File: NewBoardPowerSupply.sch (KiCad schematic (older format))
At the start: 12 parts, among them IC1 ADM7172ACPZ-4.2-R7

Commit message: getting libraries to work
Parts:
- IC1: symbol ADM7172ACPZ-4.2-R7:ADM7172ACPZ-4.2-R7 -> laser-rescue:ADM7172ACPZ-4.2-R7-ADM7172ACPZ-4.2-R7
- IC?: symbol ADM7154ARDZ-3.3-R7:ADM7154ARDZ-3.3-R7 -> laser-rescue:ADM7154ARDZ-3.3-R7-ADM7154ARDZ-3.3-R7
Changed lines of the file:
@@
 $EndDescr
 $Comp
-L ADM7172ACPZ-4.2-R7:ADM7172ACPZ-4.2-R7 IC1
+L laser-rescue:ADM7172ACPZ-4.2-R7-ADM7172ACPZ-4.2-R7 IC1
 U 1 1 60C1104B
 P 4700 4750
@@
 $EndComp
 $Comp
-L ADM7154ARDZ-3.3-R7:ADM7154ARDZ-3.3-R7 IC?
+L laser-rescue:ADM7154ARDZ-3.3-R7-ADM7154ARDZ-3.3-R7 IC?
 U 1 1 60C11888
 P 8750 4750

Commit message: delete random cashe
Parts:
- IC1: symbol laser-rescue:ADM7172ACPZ-4.2-R7-ADM7172ACPZ-4.2-R7 -> ADM7172ACPZ-4.2-R7:ADM7172ACPZ-4.2-R7
- IC?: symbol laser-rescue:ADM7154ARDZ-3.3-R7-ADM7154ARDZ-3.3-R7 -> ADM7154ARDZ-3.3-R7:ADM7154ARDZ-3.3-R7
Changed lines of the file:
@@
 $EndDescr
 $Comp
-L laser-rescue:ADM7172ACPZ-4.2-R7-ADM7172ACPZ-4.2-R7 IC1
+L ADM7172ACPZ-4.2-R7:ADM7172ACPZ-4.2-R7 IC1
 U 1 1 60C1104B
 P 4700 4750
@@
 $EndComp
 $Comp
-L laser-rescue:ADM7154ARDZ-3.3-R7-ADM7154ARDZ-3.3-R7 IC?
+L ADM7154ARDZ-3.3-R7:ADM7154ARDZ-3.3-R7 IC?
 U 1 1 60C11888
 P 8750 4750
@@
 $EndComp
 $Comp
-L _NONAME_ #PWR?
-U 1 1 60C1B1D0
-P 8750 5050
-F 0 "#PWR?" H 8750 4800 50  0001 C CNN
-F 1 "GND" H 8755 4877 50  0000 C CNN
-F 2 "" H 8750 5050 50  0001 C CNN
-F 3 "" H 8750 5050 50  0001 C CNN
-	1    8750 5050
-	1    0    0    -1
-$EndComp
-$Comp
 L Device:C C?
 U 1 1 60C28A84
@@
 Wire Wire Line
 	8400 3900 3000 3900
-Wire Wire Line
-	3000 3900 3000 4850
 Connection ~ 8400 3900
-Connection ~ 3000 4850
 Wire Wire Line
 	9000 3900 10000 3900
 Connection ~ 9000 3900
+Connection ~ 3000 4850
+Wire Wire Line
+	3000 3900 3000 4850
+$Comp
+L power:GND #PWR?
+U 1 1 60C19547
+P 8750 5050
+F 0 "#PWR?" H 8750 4800 50  0001 C CNN
+F 1 "GND" H 8755 4877 50  0000 C CNN
+F 2 "" H 8750 5050 50  0001 C CNN
+F 3 "" H 8750 5050 50  0001 C CNN
+	1    8750 5050
+	1    0    0    -1
+$EndComp
 $EndSCHEMATC

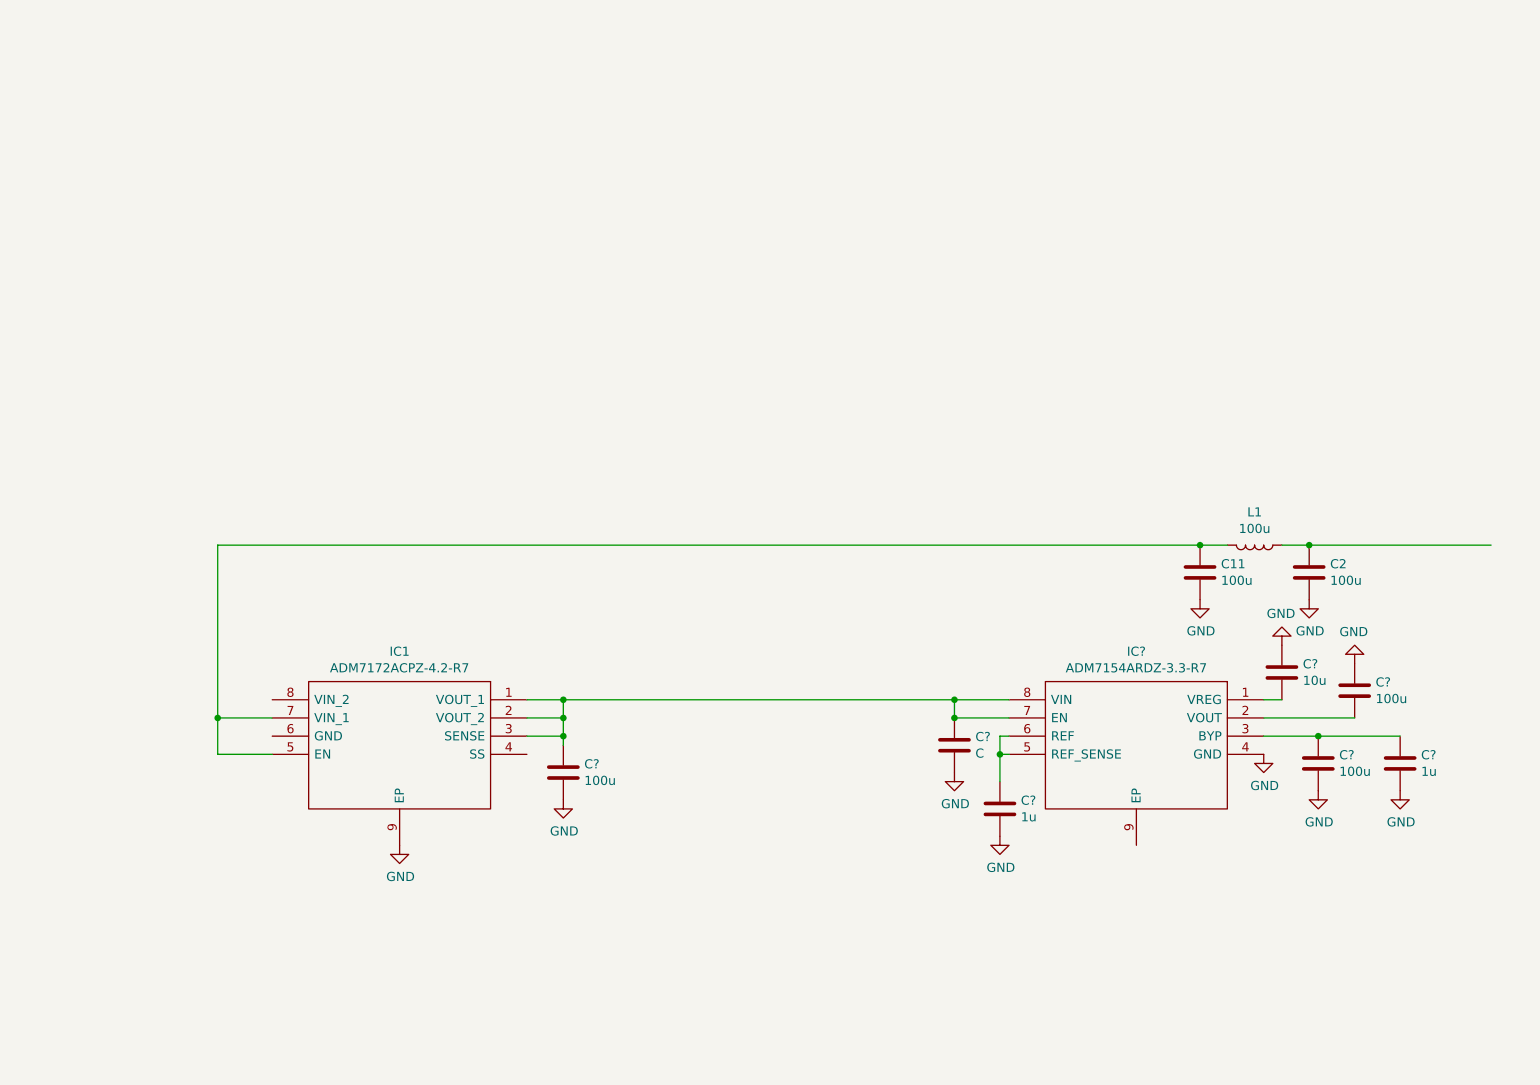
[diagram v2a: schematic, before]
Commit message: add LT1716
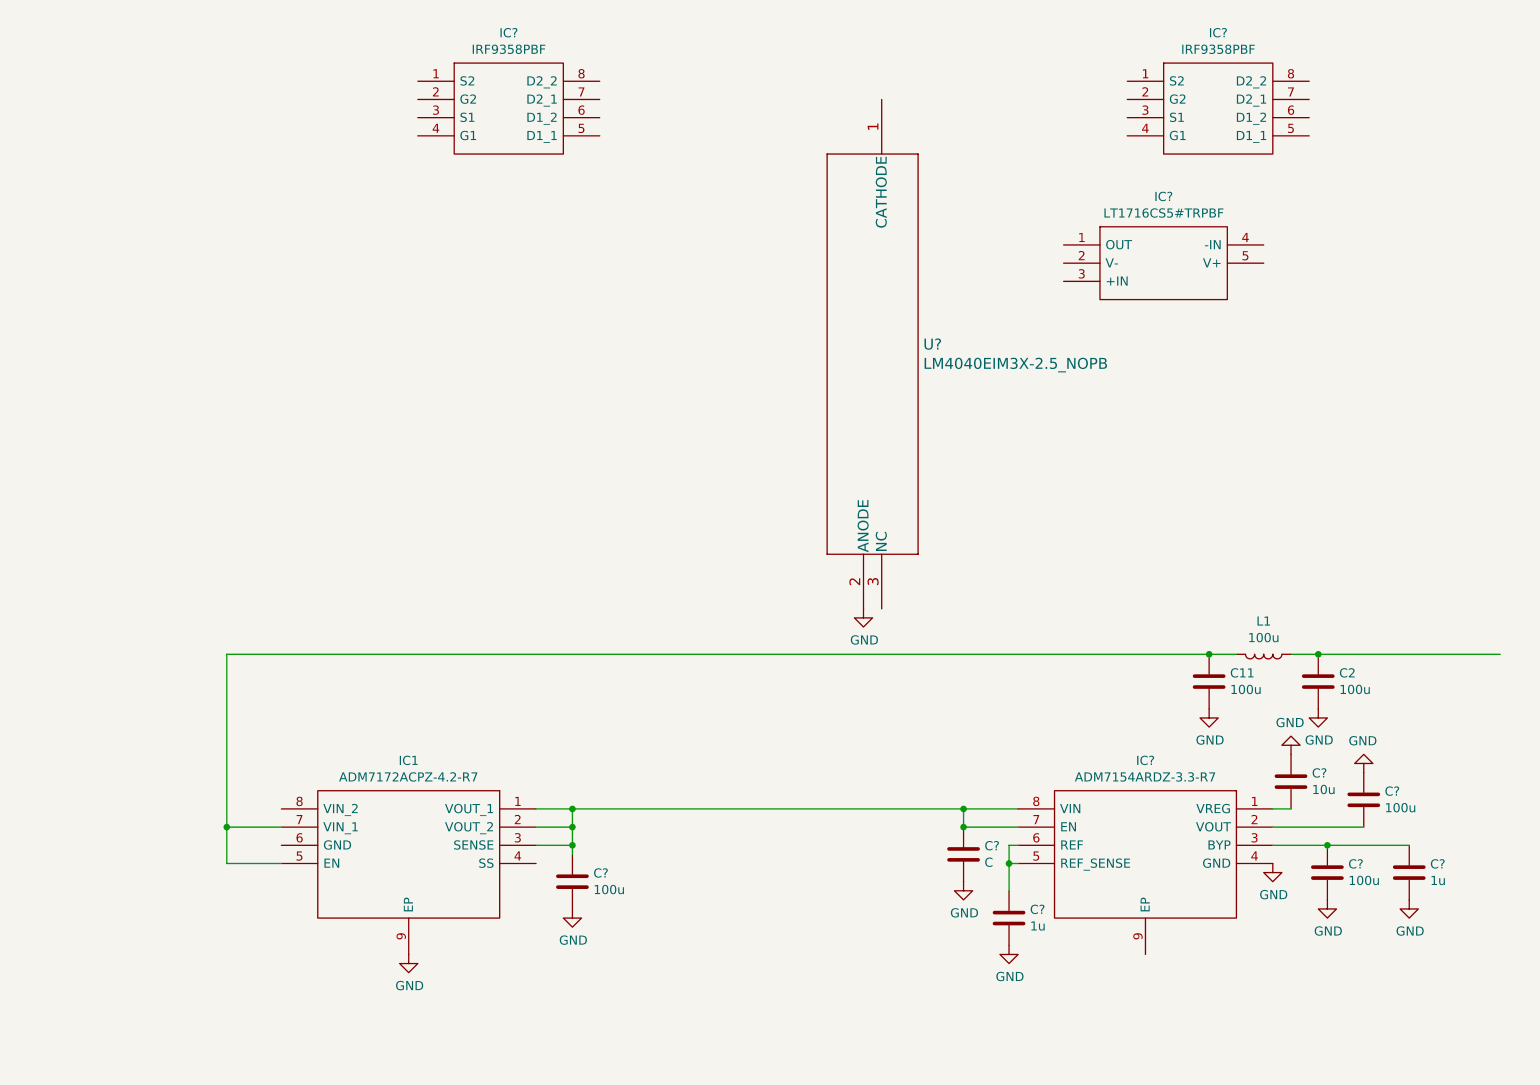
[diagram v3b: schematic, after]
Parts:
- added IC? (x2): IRF9358PBF, SOIC127P600X175-8N, symbol IRF9358PBF:IRF9358PBF
- added IC?: LT1716CS5#TRPBF, SOT95P280X100-5N, symbol LT1716CS5#TRPBF:LT1716CS5#TRPBF
- added U?: LM4040EIM3X-2.5_NOPB, DBZ3, symbol LM4040:LM4040EIM3X-2.5_NOPB
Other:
- moved on the sheet: C11, C2, C?, IC1, IC?, L1

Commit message: added labels for loose ends
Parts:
- removed IC? (x2): IRF9358PBF, SOIC127P600X175-8N, symbol IRF9358PBF:IRF9358PBF
- removed IC?: LT1716CS5#TRPBF, SOT95P280X100-5N, symbol LT1716CS5#TRPBF:LT1716CS5#TRPBF
- removed U?: LM4040EIM3X-2.5_NOPB, DBZ3, symbol LM4040:LM4040EIM3X-2.5_NOPB
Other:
- moved on the sheet: C11, C2, C?, IC1, IC?, L1

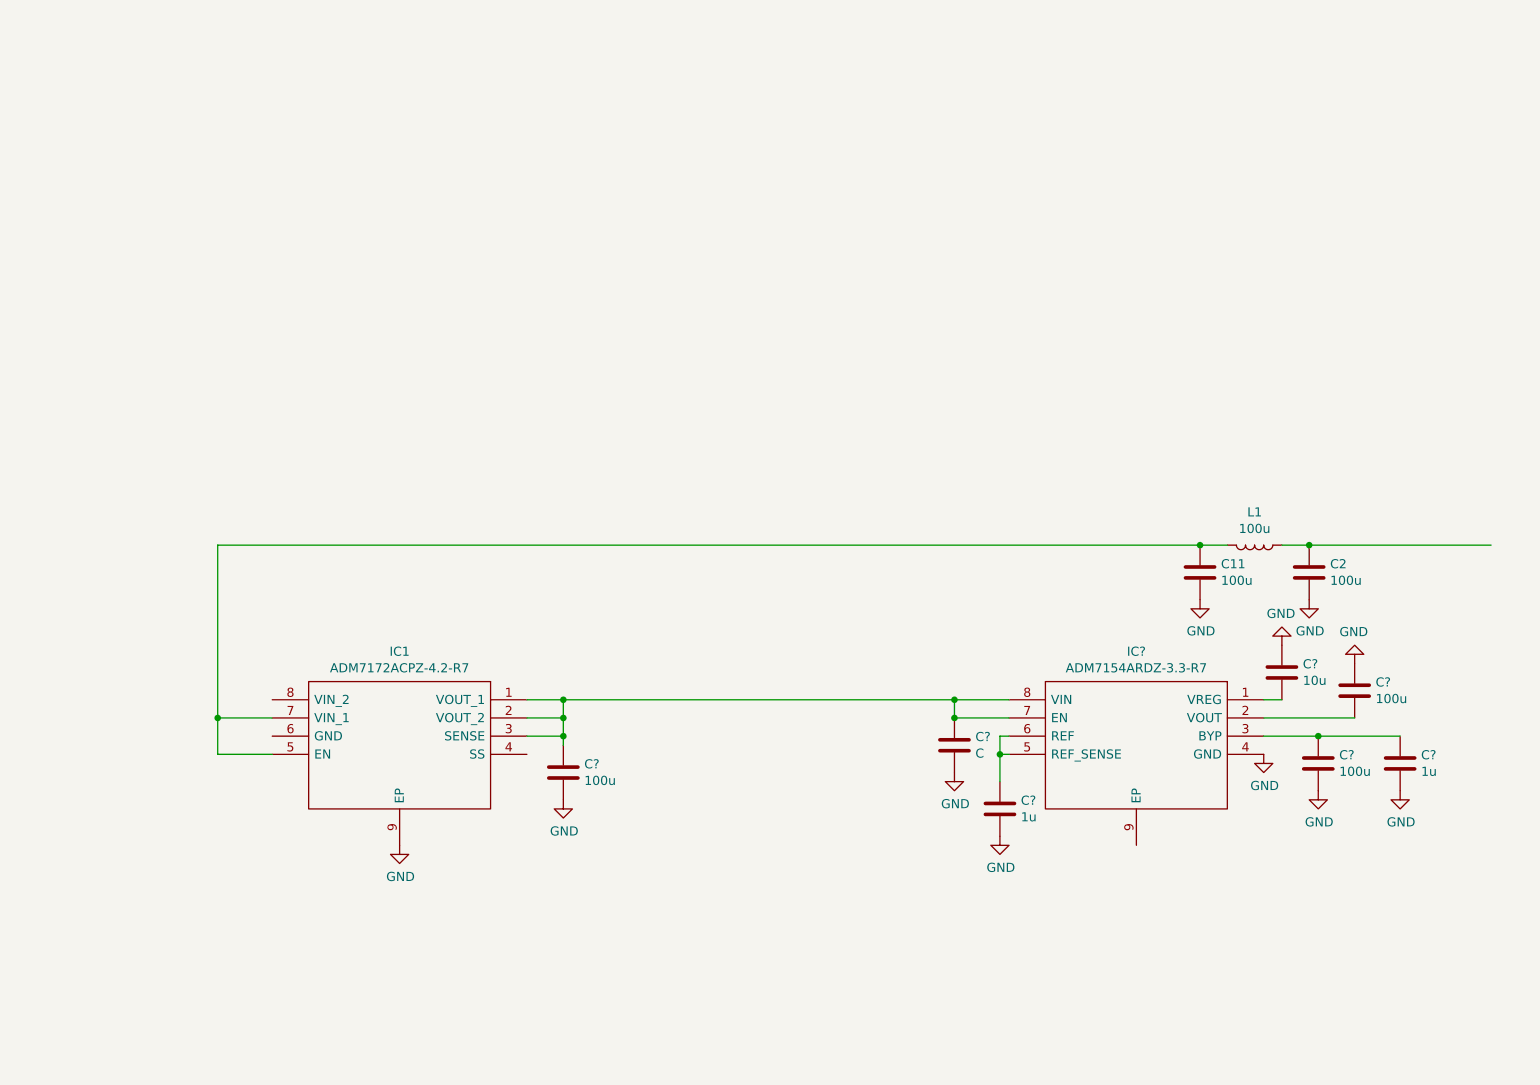
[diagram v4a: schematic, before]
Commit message: finish power supply schematic
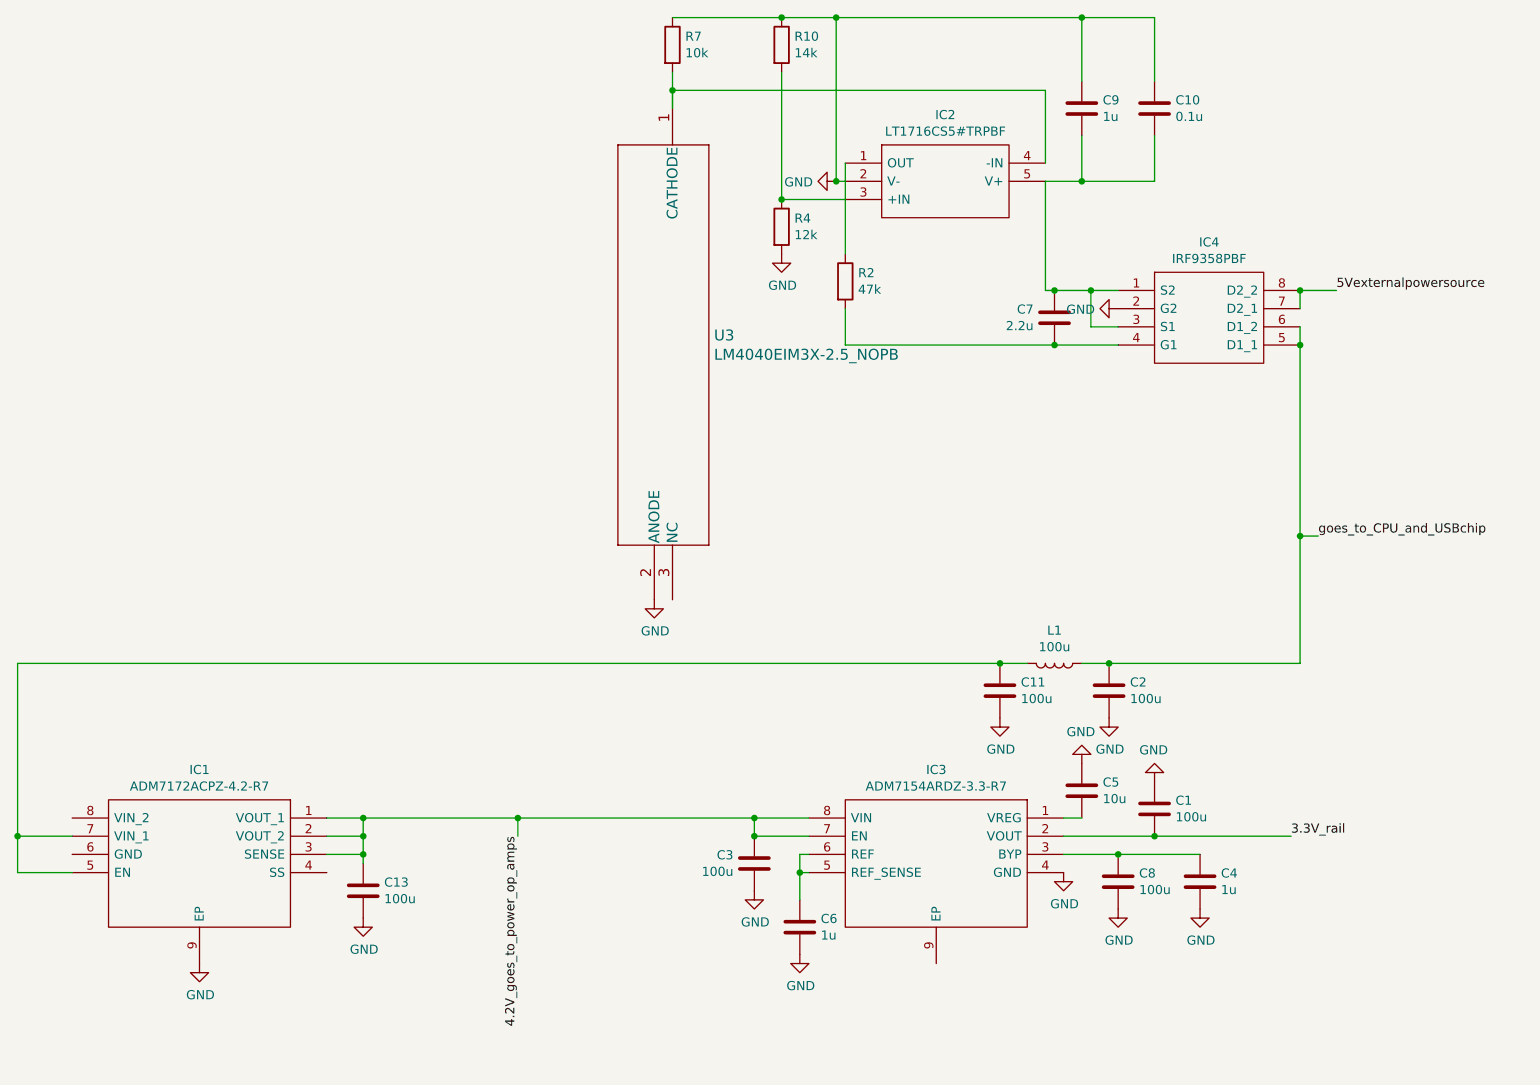
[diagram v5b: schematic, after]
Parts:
- added C10: 0.1u, symbol Device:C
- added C7: 2.2u, symbol Device:C
- added C9: 1u, symbol Device:C
- added IC2: LT1716CS5#TRPBF, SOT95P280X100-5N, symbol LT1716CS5#TRPBF:LT1716CS5#TRPBF
- added IC4: IRF9358PBF, SOIC127P600X175-8N, symbol IRF9358PBF:IRF9358PBF
- added R10: 14k, symbol Device:R
- added R2: 47k, symbol Device:R
- added R4: 12k, symbol Device:R
- added R7: 10k, symbol Device:R
- added U3: LM4040EIM3X-2.5_NOPB, DBZ3, symbol LM4040:LM4040EIM3X-2.5_NOPB
- C3: renamed from C?; value C -> 100u
- gave numbers to parts that had none: 7
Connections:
- net labels added: 3.3V_rail, 4.2V_goes_to_power_op_amps, 5Vexternalpowersource, goes_to_CPU_and_USBchip
- wire segments 26 -> 63
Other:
- moved on the sheet: C1, C11, C13, C2, C3, C4, C5, C6, C8, IC1, IC3, L1

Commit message: push final edits so i can clone
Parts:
- removed C10: 0.1u, symbol Device:C
- removed C7: 2.2u, symbol Device:C
- removed C9: 1u, symbol Device:C
- removed IC2: LT1716CS5#TRPBF, SOT95P280X100-5N, symbol LT1716CS5#TRPBF:LT1716CS5#TRPBF
- removed IC4: IRF9358PBF, SOIC127P600X175-8N, symbol IRF9358PBF:IRF9358PBF
- removed R10: 14k, symbol Device:R
- removed R2: 47k, symbol Device:R
- removed R4: 12k, symbol Device:R
- removed R7: 10k, symbol Device:R
- removed U3: LM4040EIM3X-2.5_NOPB, DBZ3, symbol LM4040:LM4040EIM3X-2.5_NOPB
- C?: renamed from C3; value 100u -> C
- renumbered C13 to C?, C4 to C?, C8 to C?, C5 to C?, C6 to C?, C1 to C?, IC3 to IC?
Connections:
- net labels removed: 3.3V_rail, 4.2V_goes_to_power_op_amps, 5Vexternalpowersource, goes_to_CPU_and_USBchip
- wire segments 63 -> 26
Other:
- moved on the sheet: C11, C2, C?, IC1, IC?, L1
